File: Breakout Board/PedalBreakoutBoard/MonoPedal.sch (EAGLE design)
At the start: 71 parts, among them IC1 LD1117V, IC2 MCP6004P, U1 OPA1652AID

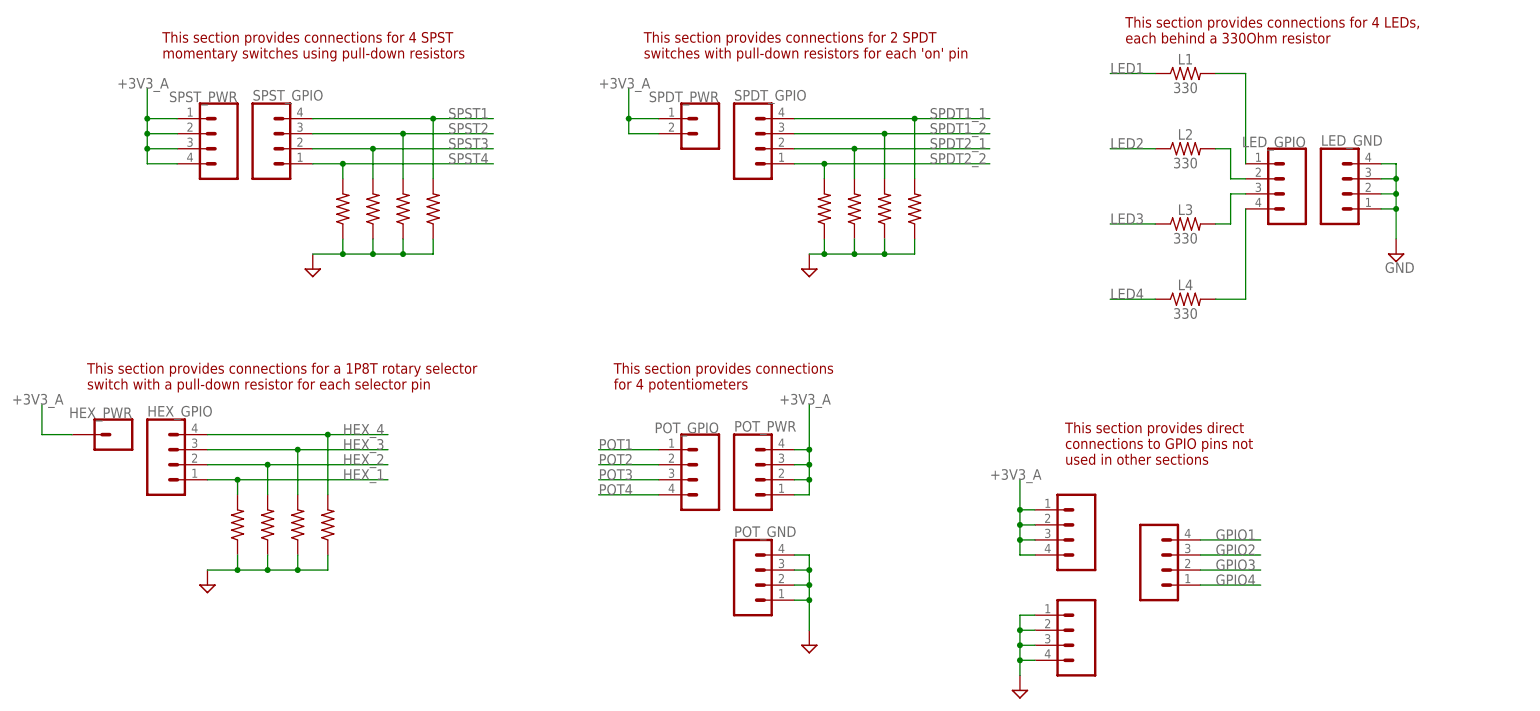
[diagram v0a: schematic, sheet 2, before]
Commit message: DP-34 - Working on board layout
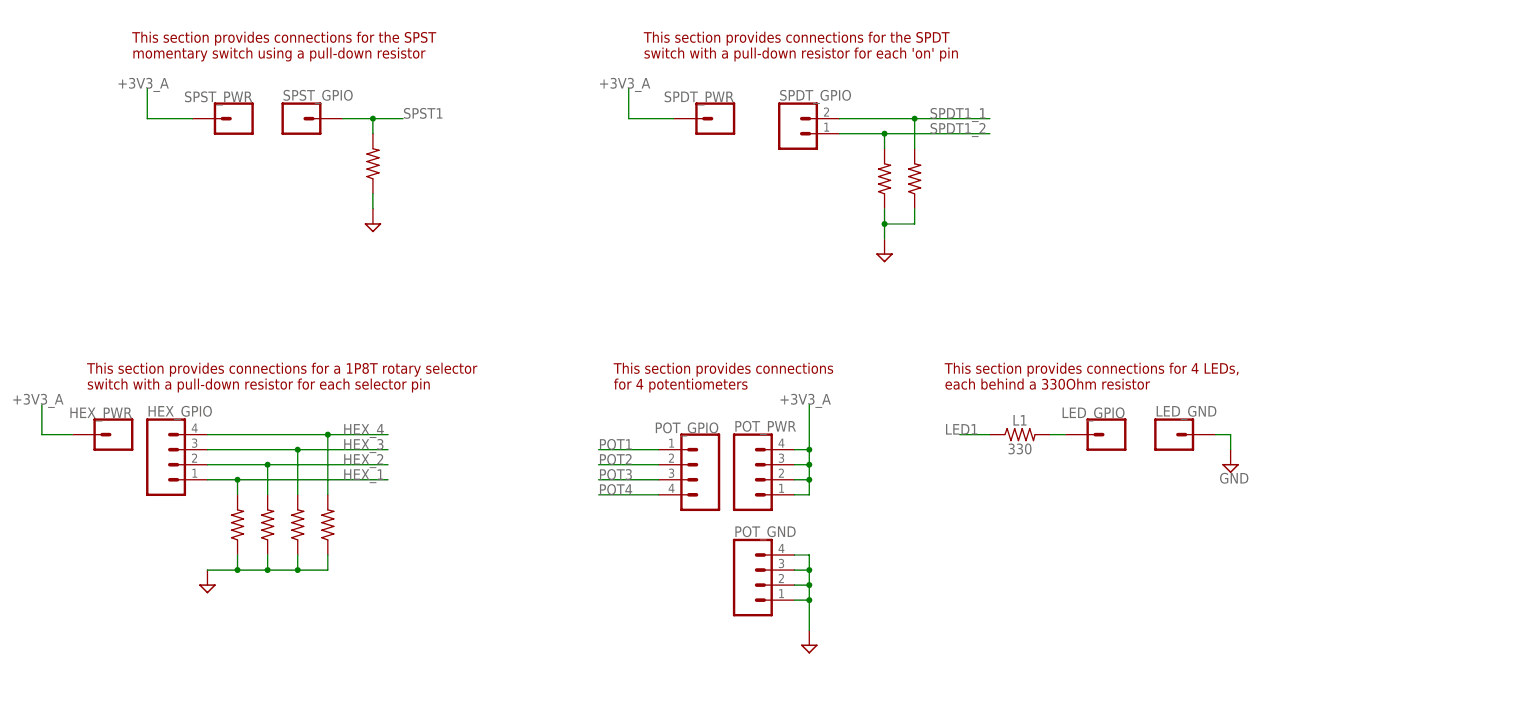
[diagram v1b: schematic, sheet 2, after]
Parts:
- removed AUDIO: (no value), SparkFun-Connectors:CONN_04X2
- removed C10, C13, C14: 10uF, SparkFun-Capacitors:10UF-POLAR-RADIAL-2.5MM-25V-20%
- removed D21, D22, S2, S3, S4: 10k, SparkFun-Resistors:10KOHM-HORIZ-1/4W-5%
- removed EX_GND, EX_GPIOS, EX_PWR: (no value), SparkFun-Connectors:CONN_04
- removed L2, L3, L4: 330, SparkFun-Resistors:330OHM-HORIZ-1/10W-5%
- removed R11, R12, R13, R14, R5, R6: 2M, Custom-Parts:2MOHM-HORIZ-1/4W-5%
- added AUD_GND, AUD_PIN: (no value), SparkFun-Connectors:CONN_02
- LED_GND, LED_GPIO, SPST_GPIO, SPST_PWR: device SparkFun-Connectors:CONN_04 -> SparkFun-Connectors:CONN_01
- SPDT_GPIO: device SparkFun-Connectors:CONN_04 -> SparkFun-Connectors:CONN_02
- SPDT_PWR: device SparkFun-Connectors:CONN_02 -> SparkFun-Connectors:CONN_01
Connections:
- removed net GPIO1: EX_GPIOS.4, SEED.GPIO1(USB_HS_ID)
- removed net GPIO2: EX_GPIOS.3, SEED.GPIO2(SDMMC1_D3)
- removed net GPIO3: EX_GPIOS.2, SEED.GPIO3(SDMMC1_D2)
- removed net GPIO4: EX_GPIOS.1, SEED.GPIO4(SDMMC1_D1)
- removed net IN_R: IC2B.-IN, IC2B.OUT, SEED.AUDIO_IN_R
- removed net IN_R_JACK: AUDIO.4, C10.-, R6.2
- removed net N$11: C10.+, IC2B.+IN, R5.1
- removed net N$16: C14.+, R13.2
- removed net N$17: R13.1, U1.INB-, U1.OUTB
- removed net N$3: L2.2, LED_GPIO.2
- removed net N$4: L3.2, LED_GPIO.3
- removed net N$5: L4.2, LED_GPIO.4
- removed net OUT_R: C13.+, SEED.AUDIO_OUT_R
- removed net OUT_R_JACK: AUDIO.8, C14.-, R14.1
- removed net SPDT2_1: D21.2, SEED.GPIO13(I2C1_SDA), SPDT_GPIO.2
- removed net SPDT2_2: D22.2, SEED.GPIO14(USART1_TX), SPDT_GPIO.1
- removed net SPST2: S2.2, SEED.GPIO7(SDMMC1_CK), SPST_GPIO.3
- removed net SPST3: S3.2, SEED.GPIO8(SPI1_NSS), SPST_GPIO.2
- removed net SPST4: S4.2, SEED.GPIO9(SPI1_SCK), SPST_GPIO.1
- new net N$18: IC2B.-IN, IC2B.OUT
- net +3V3_A: no longer EX_PWR.1, EX_PWR.2, EX_PWR.3, EX_PWR.4, SPDT_PWR.2, SPST_PWR.2, SPST_PWR.3, SPST_PWR.4
- net +5V_ISOL: no longer R11.2
- net GND: now also AUD_GND.1, AUD_GND.2, IC2B.+IN, U1.INB+; no longer AUDIO.1, AUDIO.3, AUDIO.5, AUDIO.7, D21.1, D22.1, EX_GND.1, EX_GND.2, EX_GND.3, EX_GND.4, LED_GND.2, LED_GND.3, LED_GND.4, R12.1, R14.2, R6.1, S2.1, S3.1, S4.1
- net IN_L_JACK: now also AUD_PIN.2; no longer AUDIO.2
- net LED2: no longer L2.1
- net LED3: no longer L3.1
- net LED4: no longer L4.1
- net N$15: now also U1.INB-, U1.OUTB; no longer C13.-, R11.1, R12.2, U1.INB+
- net OUT_L_JACK: now also AUD_PIN.1; no longer AUDIO.6
- net SPDT1_1: now also SPDT_GPIO.2; no longer SPDT_GPIO.4
- net SPDT1_2: now also SPDT_GPIO.1; no longer SPDT_GPIO.3
- net SPST1: now also SPST_GPIO.1; no longer SPST_GPIO.4
- net V_AUDIOBIAS: no longer R5.2
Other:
- note added: "This section provides connections for the SPDT switch with a pull-down resistor for each 'on' pin"
- note added: "This section provides connections for the SPST momentary switch using a pull-down resistor"
- note added: "Through-hole connectors wired out to 2 mono-TS jacks"
- note removed: "This section provides connections for 2 SPDT switches with pull-down resistors for each 'on' pin"
- note removed: "This section provides connections for 4 SPST momentary switches using pull-down resistors"
- note removed: "This section provides direct connections to GPIO pins not used in other sections"
- note removed: "Through-hole connectors wired out to 4 mono-TS jacks"
- moved on the sheet: C9, IC2B, IC2C, L1, R3, R4

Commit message: Working on board layout
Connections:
- removed net +3V3_D: SEED.+3V3_D
- removed net LED2: SEED.GPIO18(ADC1_INP5)
- removed net LED3: SEED.GPIO17(ADC1_INP15)
- removed net LED4: SEED.GPIO16(ADC1_INP10)
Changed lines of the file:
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@@
-</segment>
-</net>
-<net name="LED3" class="0">
-<segment>
-<pinref part="SEED" gate="G$1" pin="GPIO17(ADC1_INP15)"/>
-<wire x1="134.62" y1="71.12" x2="149.86" y2="71.12" width="0.1524" layer="91"/>
-<label x="142.24" y="71.12" size="1.778" layer="95"/>
-</segment>
-</net>
-<net name="LED4" class="0">
-<segment>
-<pinref part="SEED" gate="G$1" pin="GPIO16(ADC1_INP10)"/>
-<wire x1="134.62" y1="68.58" x2="149.86" y2="68.58" width="0.1524" layer="91"/>
-<label x="142.24" y="68.58" size="1.778" layer="95"/>
 </segment>
 </net>
@@
 <wire x1="134.62" y1="88.9" x2="149.86" y2="88.9" width="0.1524" layer="91"/>
 <label x="142.24" y="88.9" size="1.778" layer="95"/>
-</segment>
-</net>
-<net name="LED2" class="0">
-<segment>
-<pinref part="SEED" gate="G$1" pin="GPIO18(ADC1_INP5)"/>
-<wire x1="134.62" y1="73.66" x2="149.86" y2="73.66" width="0.1524" layer="91"/>
-<label x="142.24" y="73.66" size="1.778" layer="95"/>
 </segment>
 </net>
@@
 </segment>
 </net>
-<net name="+3V3_D" class="0">
-<segment>
-<pinref part="SEED" gate="G$1" pin="+3V3_D"/>
-<wire x1="134.62" y1="109.22" x2="149.86" y2="109.22" width="0.1524" layer="91"/>
-<label x="139.7" y="109.22" size="1.778" layer="95"/>
-</segment>
-</net>

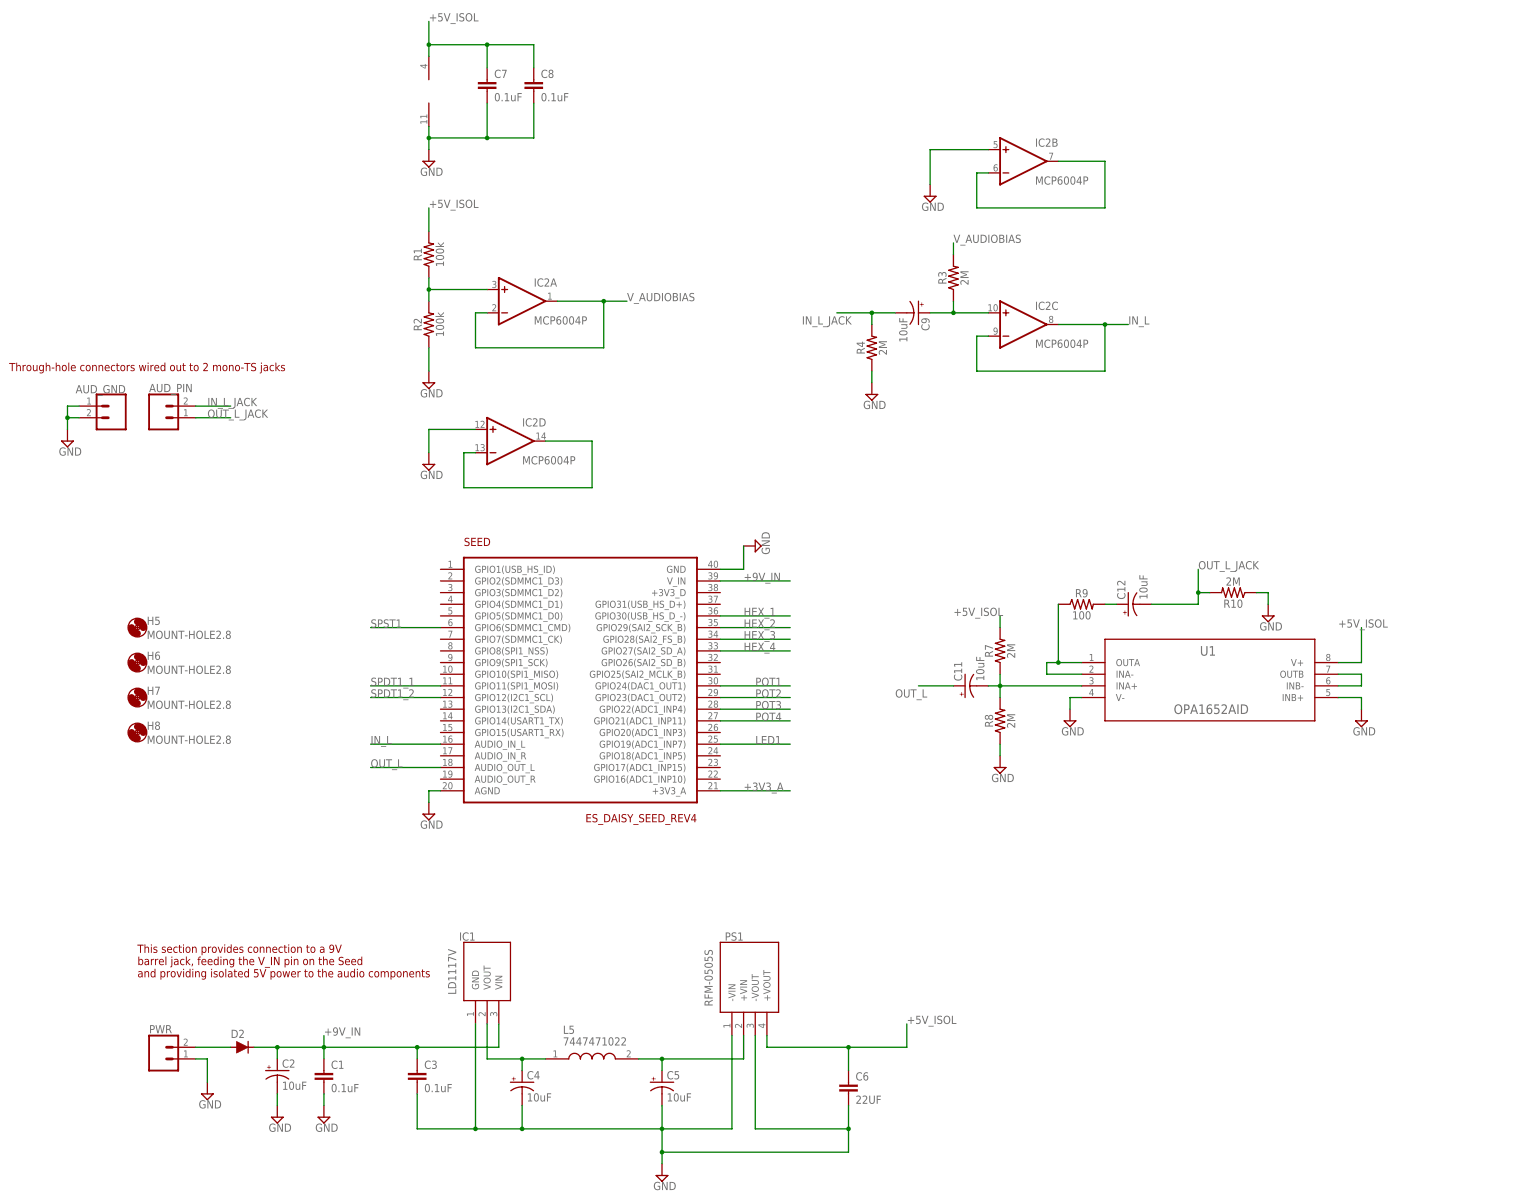
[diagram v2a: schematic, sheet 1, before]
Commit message: DP-33 - Update mono pedal to ceramic 10uF capacitors
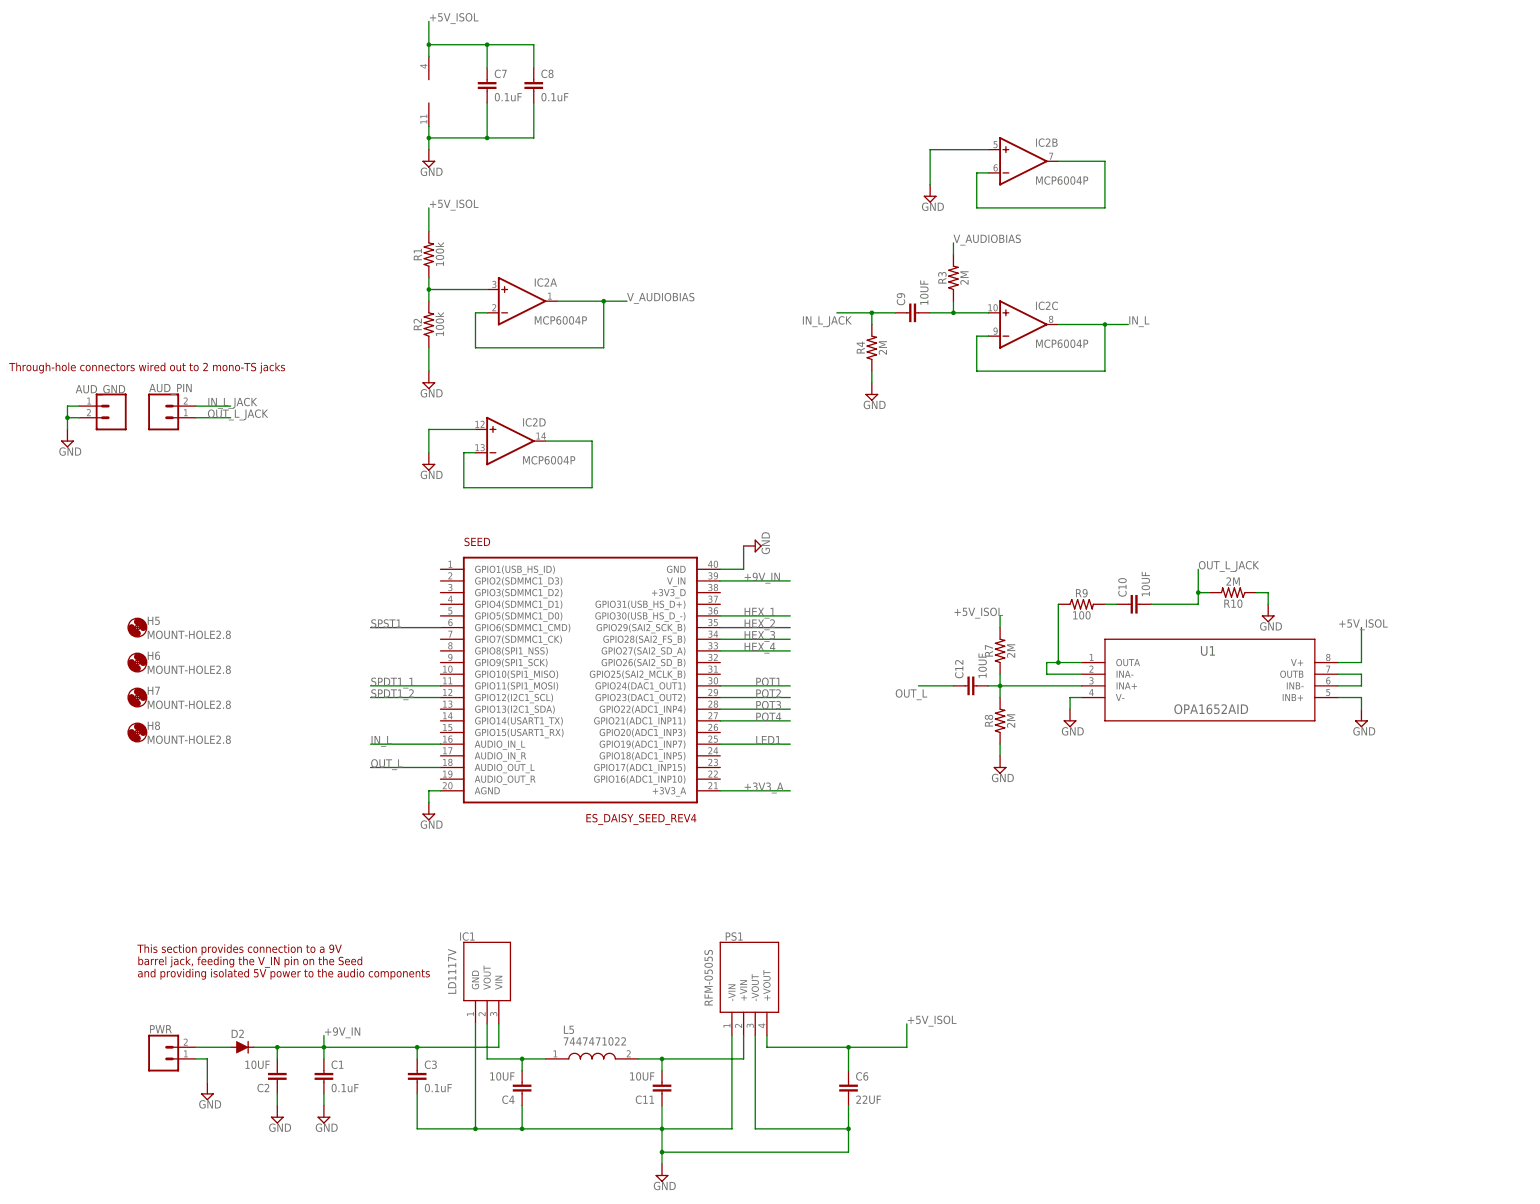
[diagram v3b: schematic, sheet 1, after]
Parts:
- removed C5: 10uF, SparkFun-Capacitors:10UF-POLAR-RADIAL-2.5MM-25V-20%
- added C10: 10UF, Custom-Parts:10UF
- C11, C12, C2, C4, C9: value 10uF -> 10UF; device SparkFun-Capacitors:10UF-POLAR-RADIAL-2.5MM-25V-20% -> Custom-Parts:10UF
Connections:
- net +9V_IN: now also C2.2; no longer C2.+
- net GND: now also C11.1, C2.1, C4.1; no longer C2.-, C4.-, C5.-
- net IN_L_JACK: now also C9.1; no longer C9.-
- net N$12: now also C12.2; no longer C11.-
- net N$14: now also C10.1; no longer C12.+
- net N$7: now also C11.2; no longer C5.+
- net N$8: now also C4.2; no longer C4.+
- net N$9: now also C9.2; no longer C9.+
- net OUT_L: now also C12.1; no longer C11.+
- net OUT_L_JACK: now also C10.2; no longer C12.-

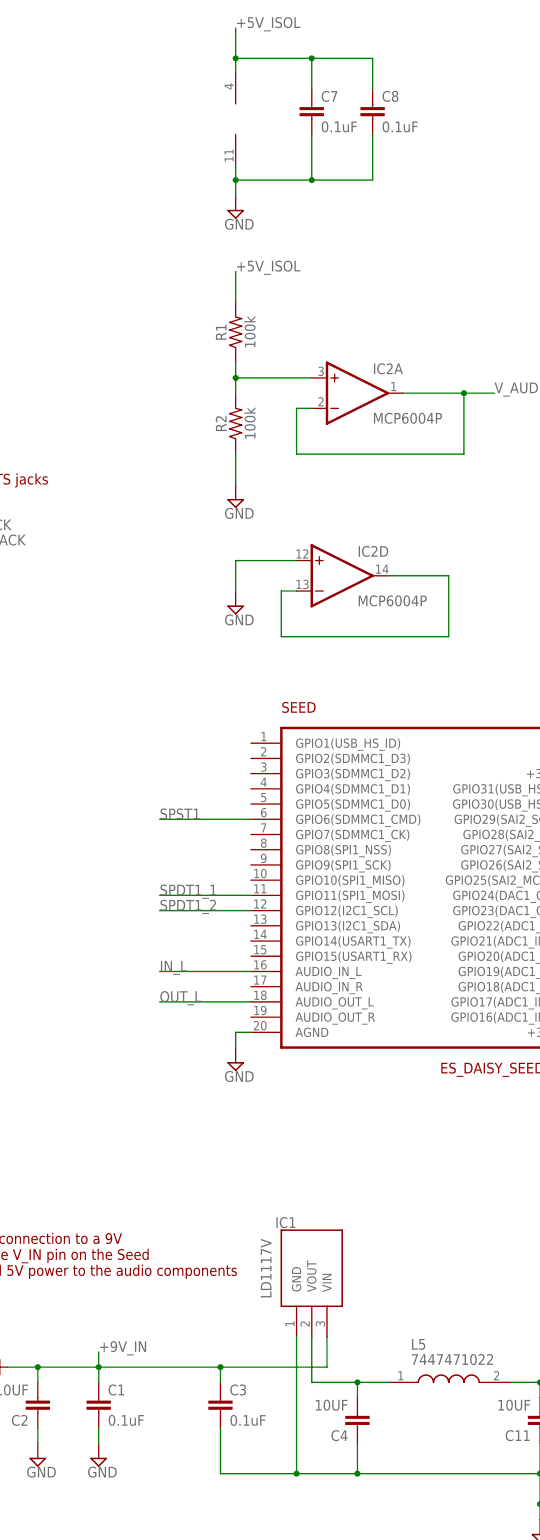
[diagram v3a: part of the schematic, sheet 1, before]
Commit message: DP-33 - Update mono pedal board with proper silk screen
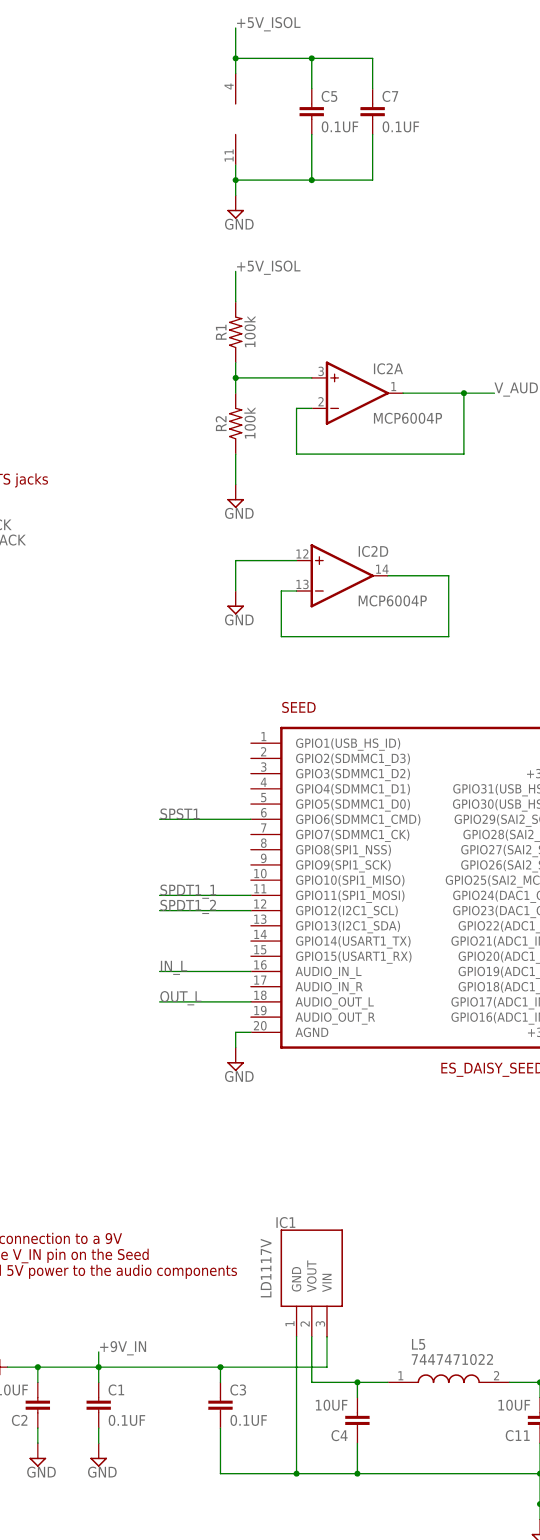
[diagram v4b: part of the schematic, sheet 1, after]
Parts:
- removed C8: 0.1uF, SparkFun-Capacitors:0.1UF-KIT-EZ-50V-20%
- added C5: 0.1UF, Custom-Parts:0.1UF
- C1, C3, C7: value 0.1uF -> 0.1UF; device SparkFun-Capacitors:0.1UF-KIT-EZ-50V-20% -> Custom-Parts:0.1UF
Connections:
- net +5V_ISOL: now also C5.1; no longer C8.1
- net GND: now also C5.2; no longer C8.2
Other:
- moved on the sheet: C7
